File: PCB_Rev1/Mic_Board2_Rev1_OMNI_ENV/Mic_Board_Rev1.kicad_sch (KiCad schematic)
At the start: 26 parts, among them J1 Conn_01x03_Pin, J2 532610771, U1 OPA1671IDBVR

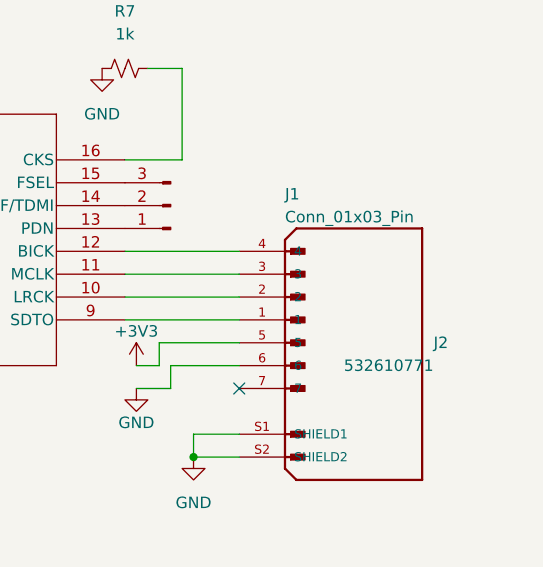
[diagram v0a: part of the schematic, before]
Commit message: MicBoard Added to MainBoard
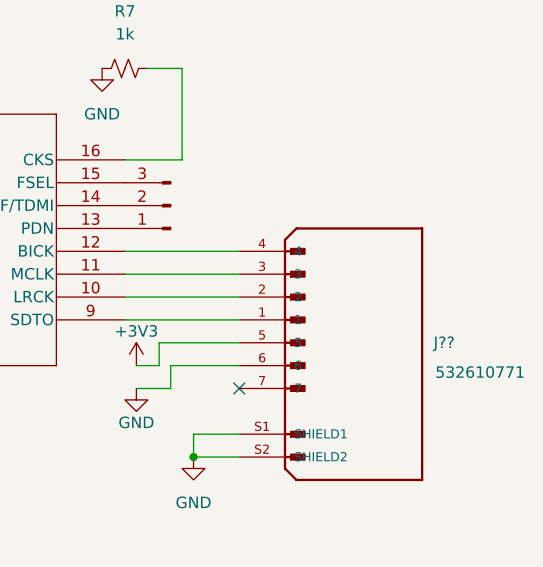
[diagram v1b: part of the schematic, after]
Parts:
- renumbered J2 to J??
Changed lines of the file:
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@@
 		(on_board yes)
 		(dnp no)
-		(property "Reference" "J2"
+		(property "Reference" "J??"
 			(at 270.51 110.49 0)
 			(effects
@@
 		)
 		(property "Value" "532610771"
-			(at 270.51 113.03 0)
+			(at 280.67 113.792 0)
 			(effects
 				(font
@@
 			(project "Mic_Board_Rev1"
 				(path "/7002bcc8-d574-4d7e-a21f-bd05f0fc5ee4"
-					(reference "J2")
+					(reference "J??")
 					(unit 1)
 				)
@@
 				)
 				(justify right)
+				(hide yes)
 			)
 		)
@@
 				)
 				(justify right)
-			)
-		)
+				(hide yes)
+			)
+		)

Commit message: Footprints
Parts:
- J71: renamed from J??; footprint cstar_mic_footprints:MOLEX_532610771 -> Footprints:HeaderConnection
- MK1: footprint cstar_mic_footprints:MIC_CMA-4544PF-W -> Footprints:Omnidirectional
- U1: footprint cstar_mic_footprints:SOT23-DBV5_TEX-L -> Footprints:Op-Amp
- U2: footprint cstar_mic_footprints:SOIC_AK5720_AKM-L -> (none)
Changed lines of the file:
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@@
 			)
 		)
-		(property "Footprint" "cstar_mic_footprints:MIC_CMA-4544PF-W"
+		(property "Footprint" "Footprints:Omnidirectional"
 			(at 34.29 92.71 0)
 			(effects
@@
 		(on_board yes)
 		(dnp no)
-		(property "Reference" "J??"
+		(property "Reference" "J71"
 			(at 270.51 110.49 0)
 			(effects
@@
 			)
 		)
-		(property "Footprint" "cstar_mic_footprints:MOLEX_532610771"
+		(property "Footprint" "Footprints:HeaderConnection"
 			(at 261.62 110.49 0)
 			(effects
@@
 			(project "Mic_Board_Rev1"
 				(path "/7002bcc8-d574-4d7e-a21f-bd05f0fc5ee4"
-					(reference "J??")
+					(reference "J71")
 					(unit 1)
 				)
@@
 			)
 		)
-		(property "Footprint" "cstar_mic_footprints:SOT23-DBV5_TEX-L"
+		(property "Footprint" "Footprints:Op-Amp"
 			(at 143.51 95.25 0)
 			(effects
@@
 			)
 		)
-		(property "Footprint" "cstar_mic_footprints:SOIC_AK5720_AKM-L"
+		(property "Footprint" ""
 			(at 185.42 90.17 0)
 			(effects
